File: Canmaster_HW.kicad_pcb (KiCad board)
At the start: 2 copper layers, 50 x 35 mm, 35 parts, among them J1 UJ2-BH-TH, J2 TC_2030_NL_STLINK, J3 Conn_01x03, M1 Mount_M3, M2 Mount_M3, M3 Mount_M3, M4 Mount_M3, U1 USBLC6-4SC6, U2 AP2139AK-3.3TRG1, U3 STM32F072CxUx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

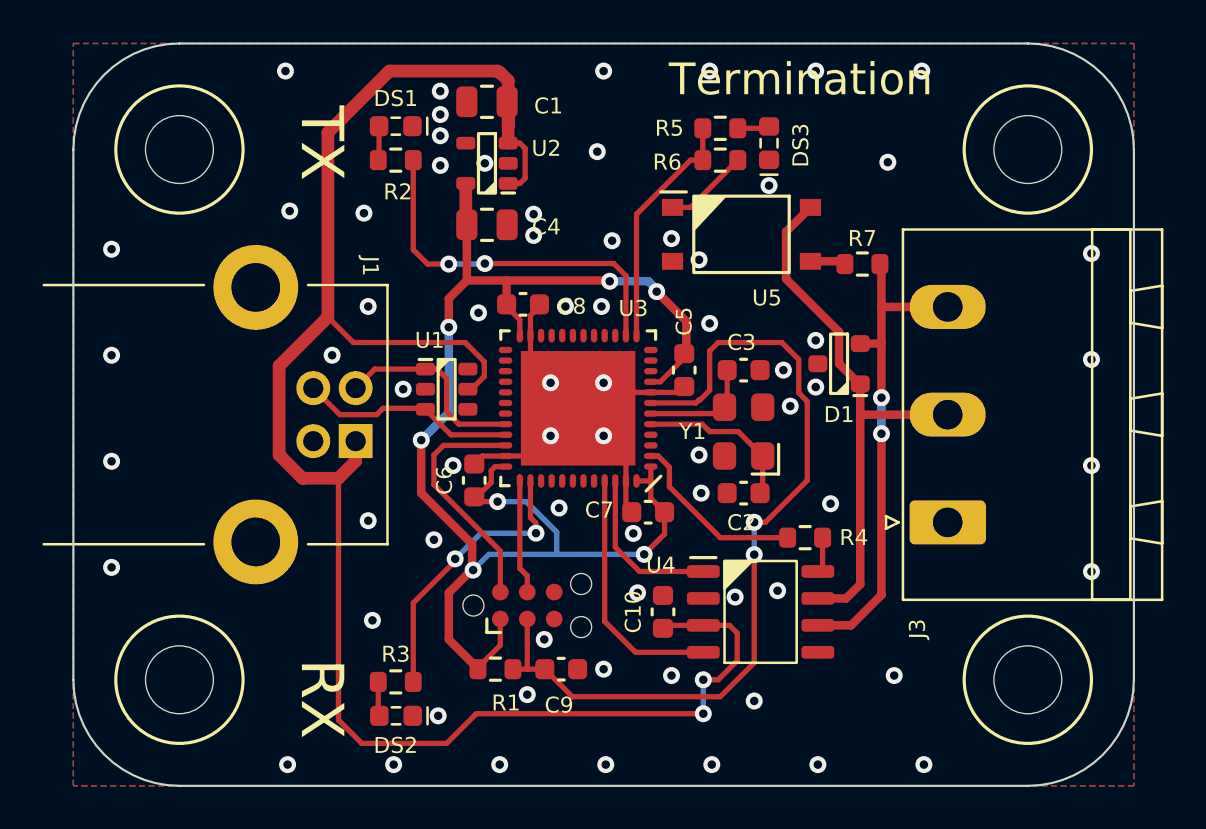
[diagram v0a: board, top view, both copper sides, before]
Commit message: Moved TX & RX LED's
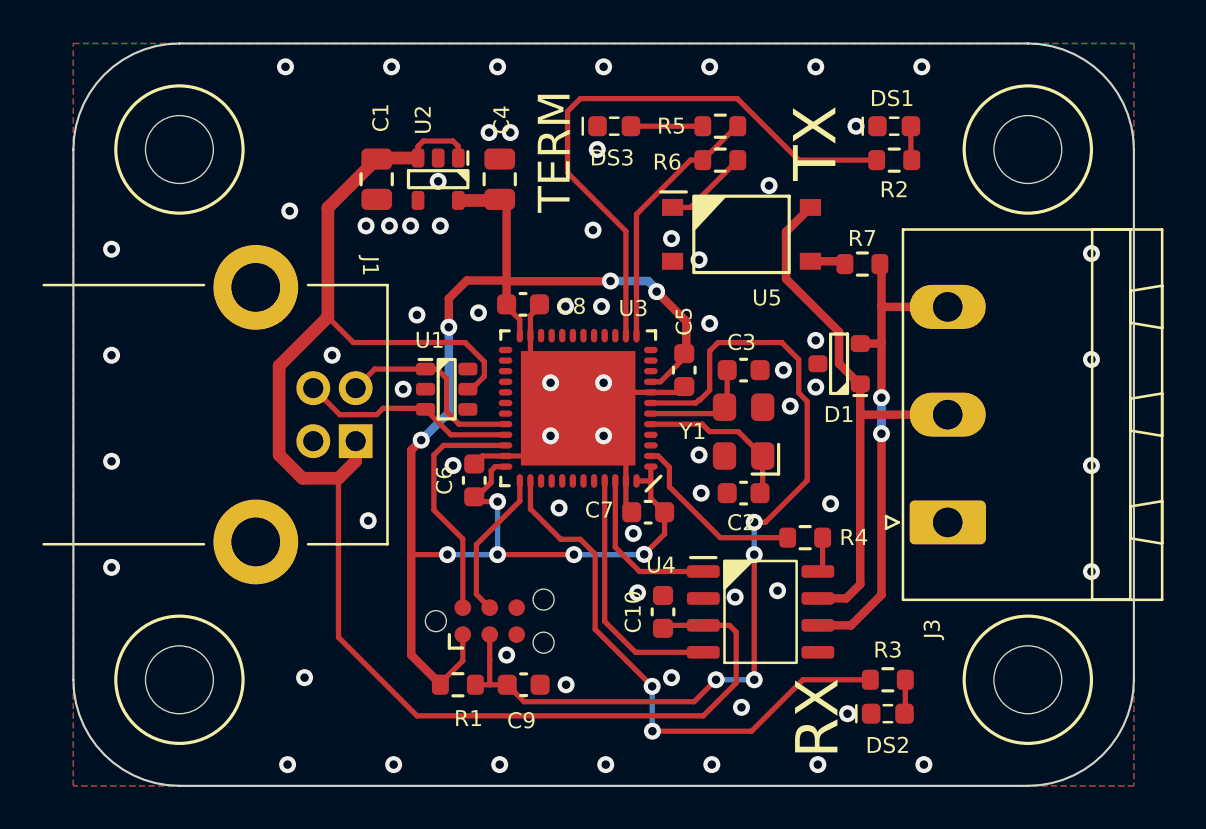
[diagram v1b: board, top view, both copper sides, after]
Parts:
- moved DS1 23.5 mm to (113.7, 58.9), turned to 0 degrees
- moved R2 23.5 mm to (113.7, 60.5), turned to 0 degrees
- moved R3 23.2 mm to (113.4, 85.0), turned to 0 degrees
- moved DS2 23.2 mm to (113.4, 86.6), turned to 0 degrees
- moved DS3 7.34 mm to (100.5, 58.9), turned to 0 degrees
- moved C1 6.35 mm to (89.3, 61.4), turned to -90 degrees
- moved U2 2.42 mm to (92.2, 61.4), turned to -90 degrees
- moved C4 2.23 mm to (95.1, 61.4), turned to 90 degrees
- moved J2 1.92 mm to (94.6, 82.2)
- moved R1 1.92 mm to (93.1, 85.2)
- moved C9 1.92 mm to (96.2, 85.2)
- moved R5 0.10 mm to (105.5, 58.9), turned to 180 degrees
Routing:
- net +5V: track 86.9 -> 70.8 mm, vias 2 -> 0
- net /MCU/LED_RX: track 13.5 -> 26.0 mm
- net /MCU/LED_TX: track 17.6 -> 27.7 mm, vias 2 -> 0
- net /MCU/NRST: track 40.3 -> 42.4 mm, vias 2 -> 4
- net Net-(DS3-Pad2): track 1.51 -> 3.39 mm
- net /MCU/SWCLK: track 5.38 -> 7.09 mm
- net +3V3: track 68.1 -> 69.4 mm, vias 7 -> 9
- net /CAN/CAN_TERM_EN: track 11.4 -> 12.2 mm
- net GND: vias 69 -> 67
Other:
- board text added: "TERM"
- board text removed: "Termination"

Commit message: Fix BOOT0 pin being disconnected
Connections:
- U3 pad 44: unconnected-(U3-Pad44) -> GND
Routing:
- net GND: track 16.3 -> 18.6 mm
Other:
- board text added: "v1.1"
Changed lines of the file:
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@@
   (net 48 "unconnected-(U3-Pad40)")
   (net 49 "unconnected-(U3-Pad41)")
-  (net 50 "unconnected-(U3-Pad44)")
-  (net 51 "/CAN/CAN_RX")
-  (net 52 "/CAN/CAN_TX")
-  (net 53 "unconnected-(U4-Pad5)")
-  (net 54 "unconnected-(U3-Pad42)")
-  (net 55 "unconnected-(U3-Pad43)")
+  (net 50 "/CAN/CAN_RX")
+  (net 51 "/CAN/CAN_TX")
+  (net 52 "unconnected-(U4-Pad5)")
+  (net 53 "unconnected-(U3-Pad42)")
+  (net 54 "unconnected-(U3-Pad43)")
   (footprint "U_IC:SOIC_8" (layer "F.Cu")
     (at 107.4 81.8)
@@
     (fp_line (start -1.95 -1.475) (end -0.975 -2.45) (layer "F.Fab") (width 0.1))
     (pad "1" smd roundrect (at -2.7 -1.905) (size 1.55 0.6) (layers "F.Cu" "F.Paste" "F.Mask") (roundrect_rratio 0.25)
-      (net 52 "/CAN/CAN_TX") (pinfunction "TXD") (pintype "output"))
+      (net 51 "/CAN/CAN_TX") (pinfunction "TXD") (pintype "output"))
     (pad "2" smd roundrect (at -2.7 -0.635) (size 1.55 0.6) (layers "F.Cu" "F.Paste" "F.Mask") (roundrect_rratio 0.25)
       (net 2 "GND") (pinfunction "VSS") (pintype "power_in"))
@@
       (net 1 "+5V") (pinfunction "VDD") (pintype "power_in"))
     (pad "4" smd roundrect (at -2.7 1.905) (size 1.55 0.6) (layers "F.Cu" "F.Paste" "F.Mask") (roundrect_rratio 0.25)
-      (net 51 "/CAN/CAN_RX") (pinfunction "RXD") (pintype "input"))
+      (net 50 "/CAN/CAN_RX") (pinfunction "RXD") (pintype "input"))
     (pad "5" smd roundrect (at 2.7 1.905) (size 1.55 0.6) (layers "F.Cu" "F.Paste" "F.Mask") (roundrect_rratio 0.25)
-      (net 53 "unconnected-(U4-Pad5)") (pinfunction "VREF") (pintype "output"))
+      (net 52 "unconnected-(U4-Pad5)") (pinfunction "VREF") (pintype "output"))
     (pad "6" smd roundrect (at 2.7 0.635) (size 1.55 0.6) (layers "F.Cu" "F.Paste" "F.Mask") (roundrect_rratio 0.25)
       (net 8 "/CAN/CAN_L") (pinfunction "CANL") (pintype "bidirectional"))
@@
       (net 2 "GND") (pinfunction "VSS") (pintype "power_in"))
     (pad "36" smd oval (at 3.425 -2.75 270) (size 0.3 0.65) (layers "F.Cu" "F.Paste" "F.Mask")
-      (net 5 "+3V3") (pinfunction "VDD") (pintype "power_in"))
+      (net 5 "+3V3") (pinfunction "VDDIO2") (pintype "power_in"))
     (pad "37" smd oval (at 2.75 -3.425 180) (size 0.3 0.65) (layers "F.Cu" "F.Paste" "F.Mask")
       (net 15 "/MCU/SWCLK") (pinfunction "SWCLK/PA14") (pintype "bidirectional"))
@@
       (net 49 "unconnected-(U3-Pad41)") (pinfunction "PB5") (pintype "bidirectional"))
     (pad "42" smd oval (at 0.25 -3.425 180) (size 0.3 0.65) (layers "F.Cu" "F.Paste" "F.Mask")
-      (net 54 "unconnected-(U3-Pad42)") (pinfunction "PB6") (pintype "bidirectional"))
+      (net 53 "unconnected-(U3-Pad42)") (pinfunction "PB6") (pintype "bidirectional"))
     (pad "43" smd oval (at -0.25 -3.425 180) (size 0.3 0.65) (layers "F.Cu" "F.Paste" "F.Mask")
-      (net 55 "unconnected-(U3-Pad43)") (pinfunction "PB7") (pintype "bidirectional"))
+      (net 54 "unconnected-(U3-Pad43)") (pinfunction "PB7") (pintype "bidirectional"))
     (pad "44" smd oval (at -0.75 -3.425 180) (size 0.3 0.65) (layers "F.Cu" "F.Paste" "F.Mask")
-      (net 50 "unconnected-(U3-Pad44)") (pinfunction "PF11") (pintype "bidirectional"))
+      (net 2 "GND") (pinfunction "BOOT0") (pintype "bidirectional"))
     (pad "45" smd oval (at -1.25 -3.425 180) (size 0.3 0.65) (layers "F.Cu" "F.Paste" "F.Mask")
-      (net 51 "/CAN/CAN_RX") (pinfunction "PB8") (pintype "bidirectional"))
+      (net 50 "/CAN/CAN_RX") (pinfunction "PB8") (pintype "bidirectional"))
     (pad "46" smd oval (at -1.75 -3.425 180) (size 0.3 0.65) (layers "F.Cu" "F.Paste" "F.Mask")
-      (net 52 "/CAN/CAN_TX") (pinfunction "PB9") (pintype "bidirectional"))
+      (net 51 "/CAN/CAN_TX") (pinfunction "PB9") (pintype "bidirectional"))
     (pad "47" smd oval (at -2.25 -3.425 180) (size 0.3 0.65) (layers "F.Cu" "F.Paste" "F.Mask")
       (net 2 "GND") (pinfunction "VSS") (pintype "power_in"))
@@
   (gr_arc (start 80 90) (mid 76.464466 88.535534) (end 75 85) (layer "Edge.Cuts") (width 0.1))
   (gr_line (start 125 85) (end 125 60) (layer "Edge.Cuts") (width 0.1))
+  (gr_text "v1.1" (at 104.7 79.8) (layer "B.SilkS")
+    (effects (font (size 2 2) (thickness 0.3)) (justify mirror))
+  )
   (gr_text "CANmaster" (at 100.5 64.7) (layer "B.SilkS")
     (effects (font (size 2 2) (thickness 0.3)) (justify mirror))
@@
   (segment (start 101.05 76.825) (end 101.325 77.1) (width 0.25) (layer "F.Cu") (net 2))
   (segment (start 101.05 75.625) (end 101.05 74.45) (width 0.25) (layer "F.Cu") (net 2))
+  (segment (start 99.55 73.95) (end 100 73.5) (width 0.25) (layer "F.Cu") (net 2))
   (segment (start 100.75 71.45) (end 100.15 70.85) (width 0.25) (layer "F.Cu") (net 2))
   (segment (start 103.8 71.175) (end 103.8 71.375) (width 0.25) (layer "F.Cu") (net 2))
@@
   (segment (start 101.05 74.45) (end 100.15 73.55) (width 0.25) (layer "F.Cu") (net 2))
   (segment (start 94.275 74.45) (end 93.9 74.825) (width 0.25) (layer "F.Cu") (net 2))
+  (segment (start 99.55 75.625) (end 99.55 73.95) (width 0.25) (layer "F.Cu") (net 2))
   (segment (start 95.375 74.45) (end 94.275 74.45) (width 0.25) (layer "F.Cu") (net 2))
   (segment (start 103.525 71.45) (end 103.8 71.175) (width 0.25) (layer "F.Cu") (net 2))
@@
   (via (at 104.6 76.2) (size 0.8) (drill 0.4) (layers "F.Cu" "B.Cu") (free) (net 2))
   (via (at 123 74.9) (size 0.8) (drill 0.4) (layers "F.Cu" "B.Cu") (free) (net 2))
-  (via (at 97.9 76.9) (size 0.8) (drill 0.4) (layers "F.Cu" "B.Cu") (free) (net 2))
+  (via (at 98.6 76.9) (size 0.8) (drill 0.4) (layers "F.Cu" "B.Cu") (free) (net 2))
   (via (at 106.2 81.1) (size 0.8) (drill 0.4) (layers "F.Cu" "B.Cu") (free) (net 2))
   (via (at 100 56.1) (size 0.8) (drill 0.4) (layers "F.Cu" "B.Cu") (free) (net 2))
@@
   (segment (start 109.75 65.27) (end 111.245 65.27) (width 0.4) (layer "F.Cu") (net 23))
   (segment (start 111.245 65.27) (end 111.375 65.4) (width 0.25) (layer "F.Cu") (net 23))
-  (segment (start 100.05 82.25) (end 101.505 83.705) (width 0.25) (layer "F.Cu") (net 51))
-  (segment (start 101.505 83.705) (end 104.7 83.705) (width 0.25) (layer "F.Cu") (net 51))
-  (segment (start 100.05 75.625) (end 100.05 82.25) (width 0.25) (layer "F.Cu") (net 51))
-  (segment (start 100.55 78.75) (end 101.695 79.895) (width 0.25) (layer "F.Cu") (net 52))
-  (segment (start 100.55 75.625) (end 100.55 78.75) (width 0.25) (layer "F.Cu") (net 52))
-  (segment (start 101.695 79.895) (end 104.7 79.895) (width 0.25) (layer "F.Cu") (net 52))
+  (segment (start 100.05 82.25) (end 101.505 83.705) (width 0.25) (layer "F.Cu") (net 50))
+  (segment (start 101.505 83.705) (end 104.7 83.705) (width 0.25) (layer "F.Cu") (net 50))
+  (segment (start 100.05 75.625) (end 100.05 82.25) (width 0.25) (layer "F.Cu") (net 50))
+  (segment (start 100.55 78.75) (end 101.695 79.895) (width 0.25) (layer "F.Cu") (net 51))
+  (segment (start 100.55 75.625) (end 100.55 78.75) (width 0.25) (layer "F.Cu") (net 51))
+  (segment (start 101.695 79.895) (end 104.7 79.895) (width 0.25) (layer "F.Cu") (net 51))
   (zone (net 2) (net_name "GND") (layers F&B.Cu) (name "GND") (hatch edge 0.508)
     (priority 1)

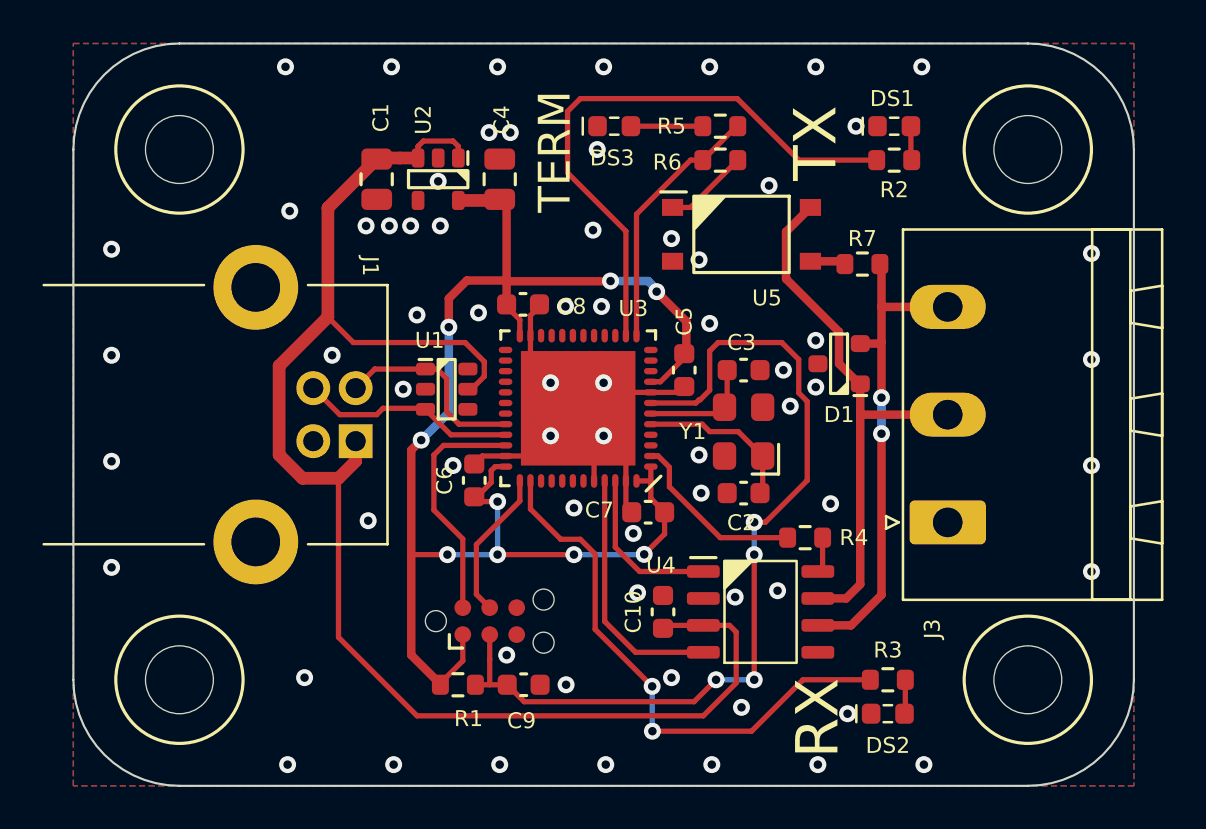
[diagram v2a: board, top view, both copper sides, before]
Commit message: Added connection for fault pin. Reversed CAN connector.
Updated some footprints
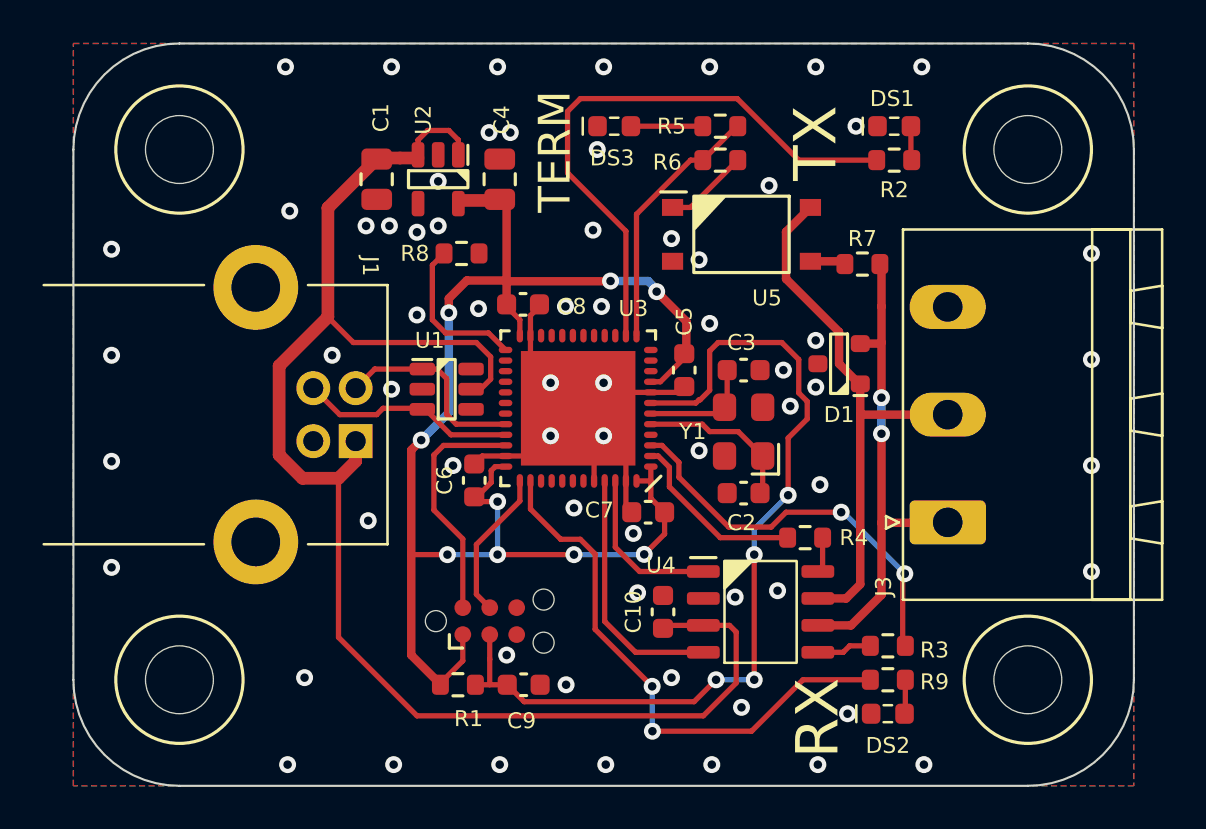
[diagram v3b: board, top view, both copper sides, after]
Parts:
- added R8: 10K, R_Resistor:R_0603, F.Cu at (93.3, 64.9)
- added R9: 0R, R_Resistor:R_0603, F.Cu at (113.4, 83.4)
- R3: value 300R -> 220R
- U2: value AP2139AK-3.3TRG1 -> NCP115ASN330T2G
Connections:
- J3 pad 1: GND -> /CAN/CAN_L
- J3 pad 3: /CAN/CAN_L -> GND
- U3 pad 25: unconnected-(U3-Pad25) -> Net-(R8-Pad2)
- U3 pad 3: unconnected-(U3-Pad3) -> /CAN/CAN_SENSE
- U4 pad 5: unconnected-(U4-Pad5) -> Net-(R9-Pad2)
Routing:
- net /CAN/CAN_SENSE: track 0.00 -> 19.0 mm, vias 0 -> 2
- net Net-(R8-Pad2): track 0.00 -> 7.39 mm
- net Net-(R9-Pad2): track 0.00 -> 2.60 mm
- net +5V: track 70.8 -> 72.2 mm
- net GND: vias 67 -> 66
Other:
- board text added: "v1.2"
- board text removed: "v1.1"

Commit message: Correct LED colors
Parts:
- DS1: value LED,YEL -> LED,RED
- DS3: value LED,RED -> LED,YEL
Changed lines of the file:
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@@
       (effects (font (size 0.75 0.75) (thickness 0.12)))
     )
-    (fp_text value "LED,YEL" (at 0 1.6) (layer "F.Fab") hide
+    (fp_text value "LED,RED" (at 0 1.6) (layer "F.Fab") hide
       (effects (font (size 1 1) (thickness 0.15)))
     )
@@
       (effects (font (size 0.75 0.75) (thickness 0.12)))
     )
-    (fp_text value "LED,RED" (at 0 1.6) (layer "F.Fab") hide
-      (effects (font (size 1 1) (thickness 0.15)))
-    )
+    (fp_text value "LED,YEL" (at 0 1.6) (layer "F.Fab") hide
+      (effects (font (size 1 1) (thickness 0.15)))
+    )
